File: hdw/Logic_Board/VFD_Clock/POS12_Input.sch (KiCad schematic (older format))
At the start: 29 parts

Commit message: Added display board schematic, other additions to logic board
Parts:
- removed C?: C, symbol Custom_Library:CP_Tant_Custom
- removed D?: D_TVS_ALT, symbol Device:D_TVS_ALT
- added C?: 100uF, Capacitors_Tantalum_SMD:CP_Tantalum_Case-X_EIA-7343-43_Reflow, symbol Custom_Library:CP_Tant_Custom
- added D?: 24V, Diodes_SMD:D_SMA, symbol Device:D_TVS_ALT
- J?: value +24V IN -> +12V IN
- R?: value 1.3M -> 6.04M
- R?: value 4.64k -> 86.6k
- R?: value 25.5k -> 243k
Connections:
- net labels added: +12V, POS12_ISNS, POS12_PGOOD
- net labels removed: +24V, +24Vin, POS24_ISNS, POS24_PGOOD
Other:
- note added: "UVLO threshold set to 10V\nOVLO threshold set to 14V"
- note removed: "UVLO threshold set to 22V\nOVLO threshold set to 26V"

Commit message: Resurrected project
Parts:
- removed C?: 0.1uF, Capacitors_SMD:C_0603, symbol Custom_Library:C_Custom
- removed C?: 10nF, Capacitors_SMD:C_0603, symbol Custom_Library:C_Custom
- removed C? (x2): 1nF, Capacitors_SMD:C_0603, symbol Custom_Library:C_Custom
- removed R?: 499k, Resistors_SMD:R_0603, symbol Custom_Library:R_Custom
- removed TP?: TP, Pin_Headers:Pin_Header_Angled_1x01_Pitch2.54mm, symbol Custom_Library:TP
- removed U?: INA138, TO_SOT_Packages_SMD:SOT-23-5, symbol Amplifier_Current:INA138
- added C?: 0.1uF, Capacitors_SMD:C_0603, symbol Custom_Library:C_Custom
- added R? (x2): 10, Resistors_SMD:R_0603, symbol Custom_Library:R_Custom
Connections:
- net +12V: now also R?.2
- net at Q?.5 (D), R?.1, U?.6 (Vout): now also R?.2
- new net POS12_SNS_+: C?.1, R?.1
- new net POS12_SNS_-: C?.2, R?.1
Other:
- note removed: "1.996 V/A"
- moved on the sheet: C?, R?, TP?

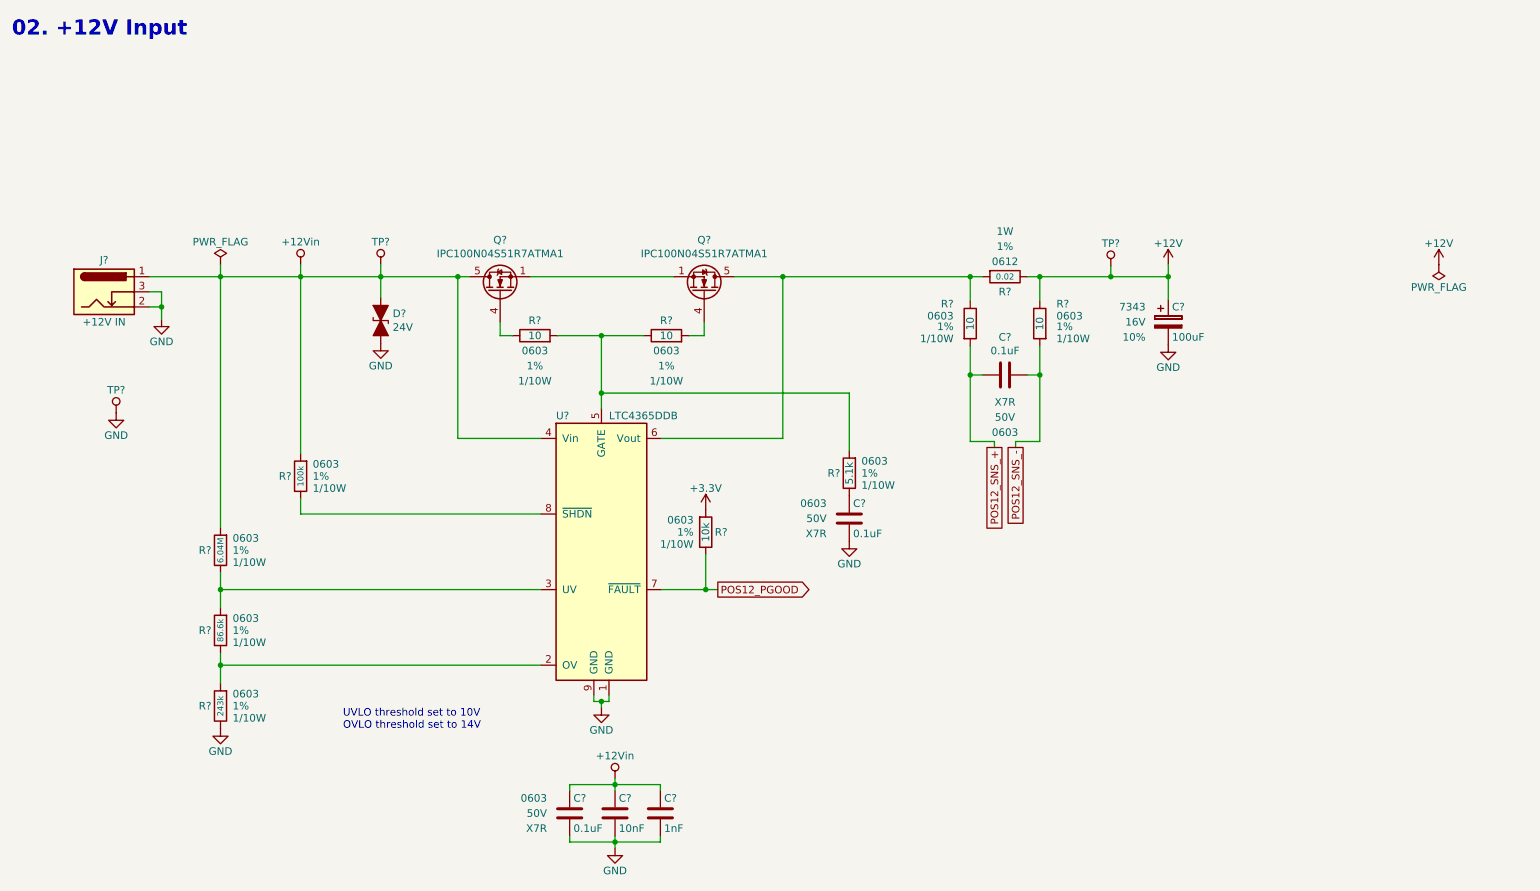
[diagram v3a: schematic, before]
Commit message: Power supply additions
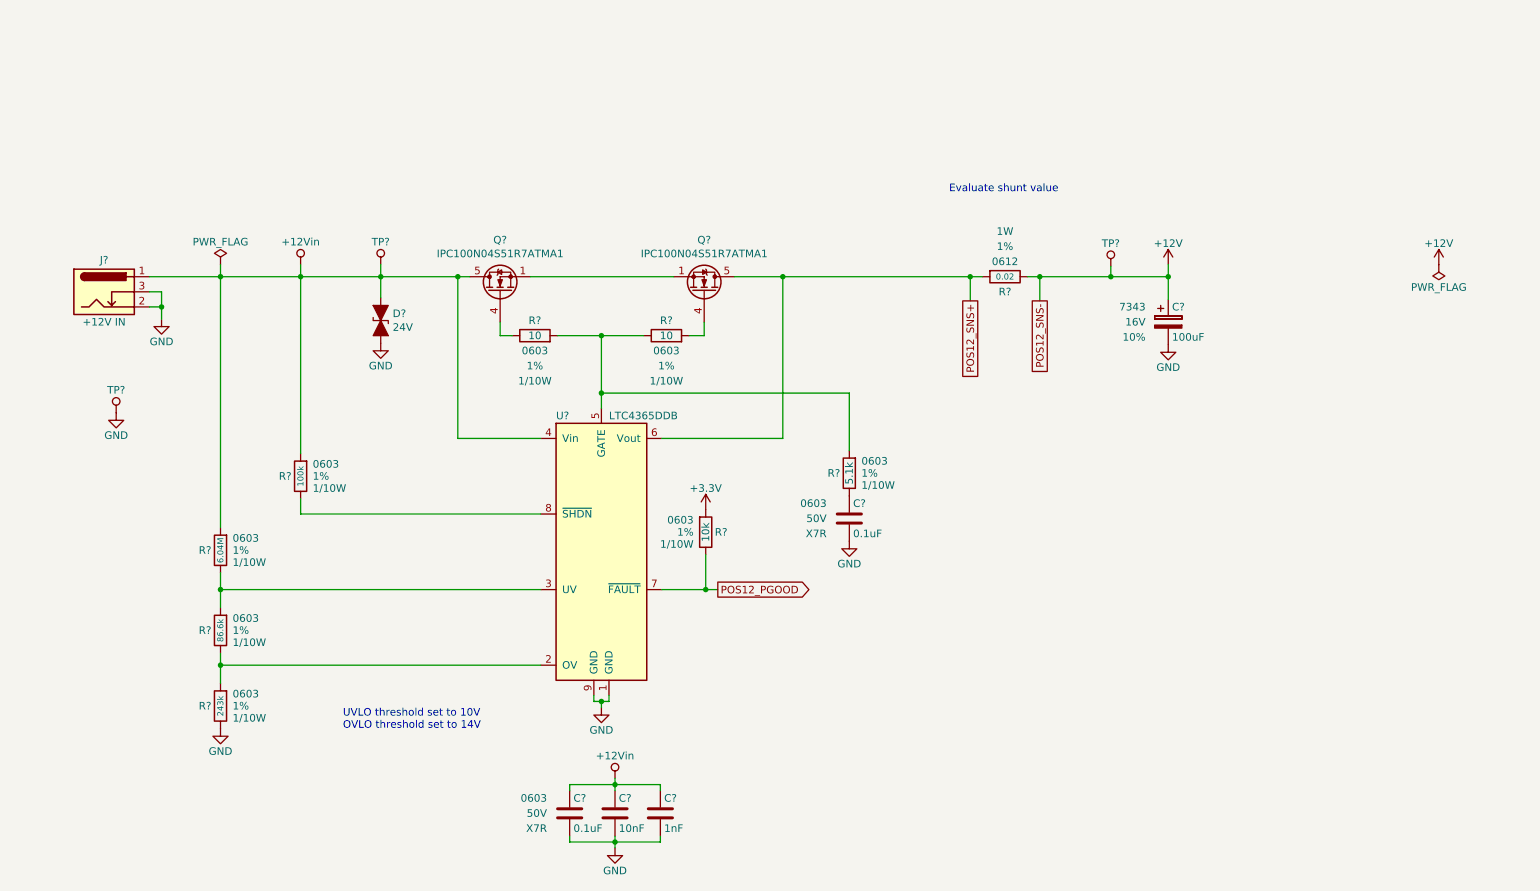
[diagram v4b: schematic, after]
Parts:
- removed C?: 0.1uF, Capacitors_SMD:C_0603, symbol Custom_Library:C_Custom
- removed R? (x2): 10, Resistors_SMD:R_0603, symbol Custom_Library:R_Custom
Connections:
- net POS12_SNS+: now reaches Q?.5 (D), R?.1, U?.6 (Vout)
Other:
- note added: "Evaluate shunt value"
- note removed: "02. +12V Input"
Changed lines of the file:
@@
 $Descr A 11000 8500
 encoding utf-8
-Sheet 16 20
+Sheet 14 25
 Title "QI Charger"
 Date "2019-01-03"
@@
 	7810 2200 7810 2270
 Connection ~ 7810 2270
-Text Notes 540  690  0    100  ~ 20
-02. +12V Input
 $Comp
 L power:+3.3V #PWR?
@@
 $EndComp
 Connection ~ 5640 2270
-Text GLabel 7040 3400 3    50   UnSpc ~ 0
-POS12_SNS_+
-Text GLabel 7180 3400 3    50   UnSpc ~ 0
-POS12_SNS_-
-$Comp
-L Custom_Library:R_Custom R?
-U 1 1 5E074F62
-P 6880 2580
-F 0 "R?" H 6990 2450 50  0000 L CNN
-F 1 "10" V 6880 2580 50  0000 C CNN
-F 2 "Resistors_SMD:R_0603" H 6880 2580 50  0001 C CNN
-F 3 "" H 6880 2580 50  0001 C CNN
-F 4 "YAG3351CT-ND" H 7180 2980 60  0001 C CNN "Digi-Key PN"
-F 5 "0603" H 6990 2530 50  0000 L CNN "display_footprint"
-F 6 "1%" H 6990 2600 50  0000 L CNN "Tolerance"
-F 7 "1/10W" H 6990 2680 50  0000 L CNN "Wattage"
-	1    6880 2580
-	-1   0    0    1
-$EndComp
-$Comp
-L Custom_Library:R_Custom R?
-U 1 1 5E076BDD
-P 7340 2580
-F 0 "R?" H 7450 2450 50  0000 L CNN
-F 1 "10" V 7340 2580 50  0000 C CNN
-F 2 "Resistors_SMD:R_0603" H 7340 2580 50  0001 C CNN
-F 3 "" H 7340 2580 50  0001 C CNN
-F 4 "YAG3351CT-ND" H 7640 2980 60  0001 C CNN "Digi-Key PN"
-F 5 "0603" H 7450 2530 50  0000 L CNN "display_footprint"
-F 6 "1%" H 7450 2600 50  0000 L CNN "Tolerance"
-F 7 "1/10W" H 7450 2680 50  0000 L CNN "Wattage"
-	1    7340 2580
-	1    0    0    1
-$EndComp
-$Comp
-L Custom_Library:C_Custom C?
-U 1 1 5E0794C5
-P 7110 2920
-AR Path="/5BAAE16C/5E0794C5" Ref="C?"  Part="1"
-AR Path="/5BB181D8/5E0794C5" Ref="C?"  Part="1"
-AR Path="/5BB2595E/5E0794C5" Ref="C?"  Part="1"
-AR Path="/5BAAE0FA/5E0794C5" Ref="C?"  Part="1"
-AR Path="/5BB86F23/5E0794C5" Ref="C?"  Part="1"
-AR Path="/5C1D5C9E/5E0794C5" Ref="C?"  Part="1"
-AR Path="/5CB6F1ED/5E0794C5" Ref="C?"  Part="1"
-F 0 "C?" V 7360 2920 50  0000 C CNN
-F 1 "0.1uF" V 7270 2920 50  0000 C CNN
-F 2 "Capacitors_SMD:C_0603" H 7148 2770 50  0001 C CNN
-F 3 "" H 7135 3020 50  0001 C CNN
-F 4 "0603" V 6730 2920 50  0000 C CNN "display_footprint"
-F 5 "50V" V 6830 2920 50  0000 C CNN "Voltage"
-F 6 "X7R" V 6930 2920 50  0000 C CNN "Dielectric"
-F 7 "311-1344-1-ND" H 7535 3420 60  0001 C CNN "Digi-Key PN"
-	1    7110 2920
-	0    -1   -1   0
-$EndComp
-Wire Wire Line
-	6880 2730 6880 2920
-Wire Wire Line
-	6880 2920 6960 2920
-Wire Wire Line
-	7260 2920 7340 2920
-Wire Wire Line
-	7340 2920 7340 2730
-Wire Wire Line
-	6880 2920 6880 3360
-Wire Wire Line
-	6880 3360 7040 3360
-Wire Wire Line
-	7040 3360 7040 3400
-Connection ~ 6880 2920
-Wire Wire Line
-	7340 2920 7340 3360
-Wire Wire Line
-	7340 3360 7180 3360
-Wire Wire Line
-	7180 3360 7180 3400
-Connection ~ 7340 2920
 Wire Wire Line
 	5640 2270 6880 2270
@@
 Wire Wire Line
 	6880 2270 6960 2270
+Text Notes 6740 1720 0    50   ~ 0
+Evaluate shunt value
+Text GLabel 7340 2430 3    50   UnSpc ~ 0
+POS12_SNS-
+Text GLabel 6880 2430 3    50   UnSpc ~ 0
+POS12_SNS+
 $EndSCHEMATC

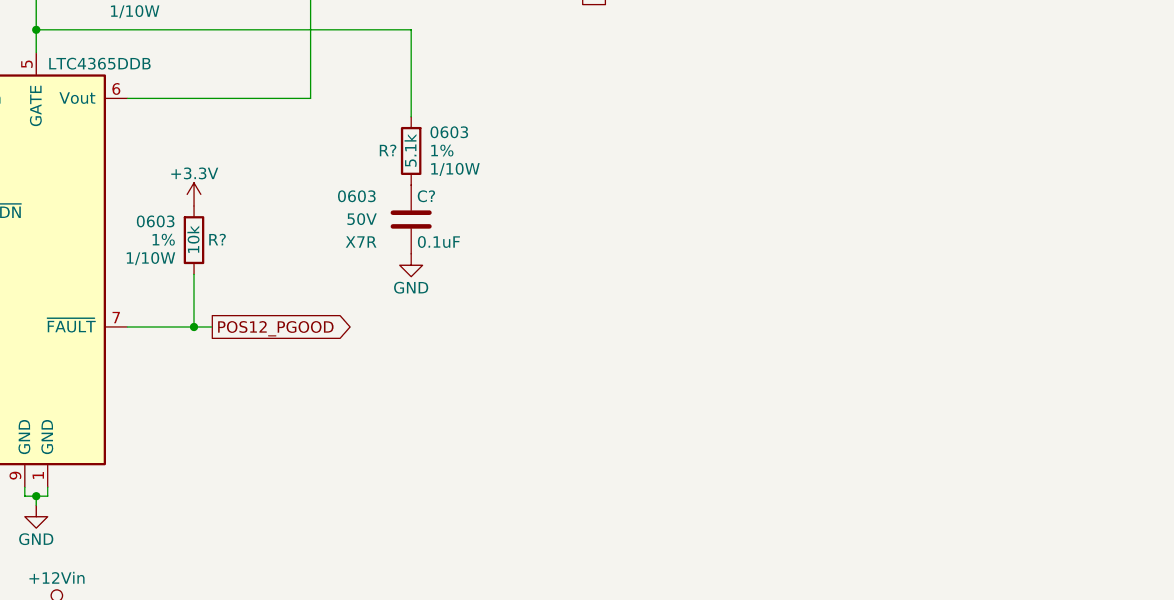
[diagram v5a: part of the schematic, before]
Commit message: Lots of schematic additions
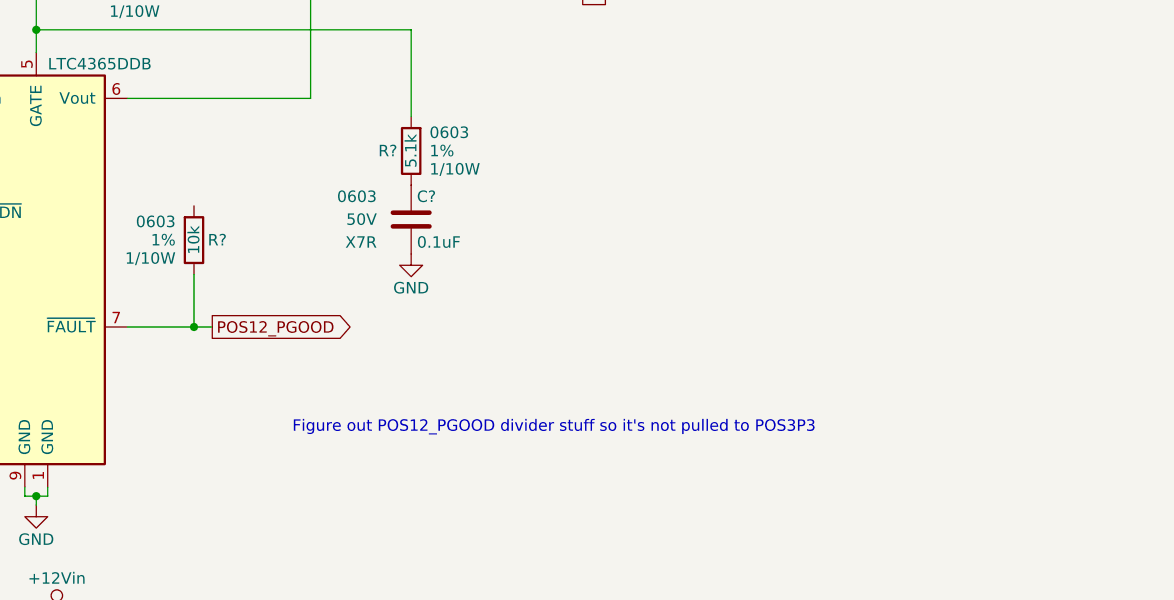
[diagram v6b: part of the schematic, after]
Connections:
- net +3V3: no longer names the net of R?.1
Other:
- note added: "Figure out POS12_PGOOD divider stuff so it's not pulled to POS3P3"
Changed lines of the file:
@@
 $Descr A 11000 8500
 encoding utf-8
-Sheet 14 26
+Sheet 14 28
 Title "QI Charger"
 Date "2019-01-03"
@@
 	7810 2200 7810 2270
 Connection ~ 7810 2270
-$Comp
-L power:+3.3V #PWR?
-U 1 1 5CB6E44A
-P 5130 3810
-F 0 "#PWR?" H 5130 3660 50  0001 C CNN
-F 1 "+3.3V" H 5130 3950 50  0000 C CNN
-F 2 "" H 5130 3810 50  0001 C CNN
-F 3 "" H 5130 3810 50  0001 C CNN
-	1    5130 3810
-	1    0    0    -1
-$EndComp
 Connection ~ 5640 2270
 Wire Wire Line
@@
 Text GLabel 6880 2430 3    50   UnSpc ~ 0
 POS12_SNS+
+Text Notes 5560 4810 0    50   ~ 0
+Figure out POS12_PGOOD divider stuff so it's not pulled to POS3P3
 $EndSCHEMATC

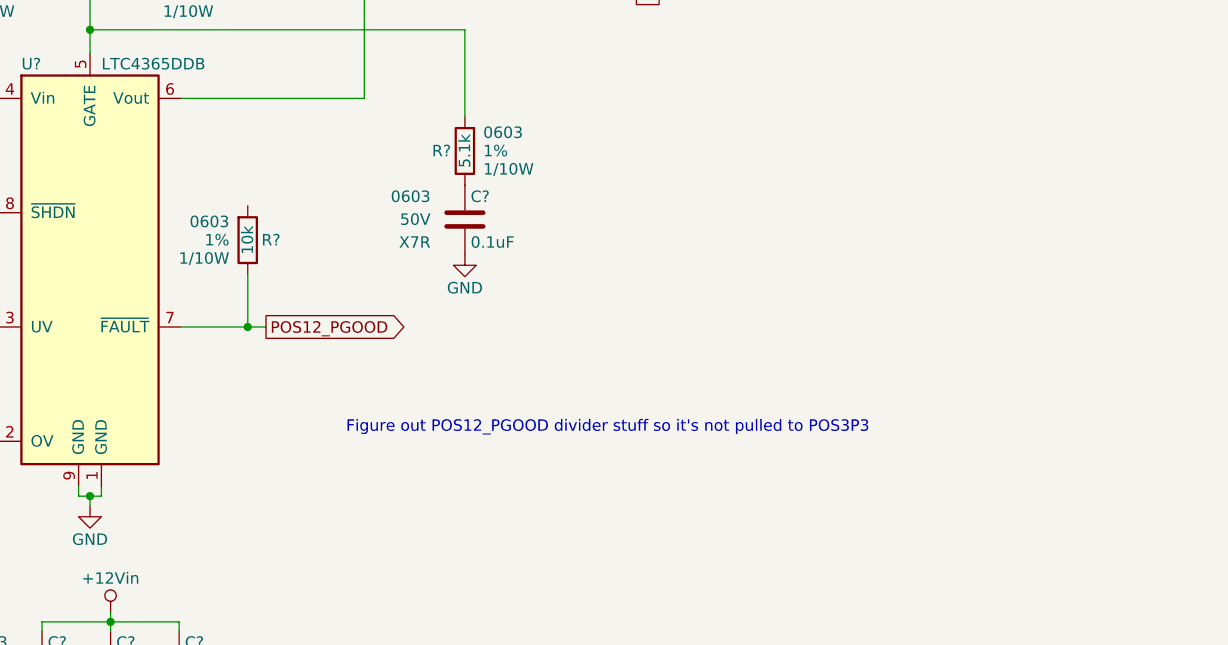
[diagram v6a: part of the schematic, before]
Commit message: Started IV-6 display board, continued logic board development
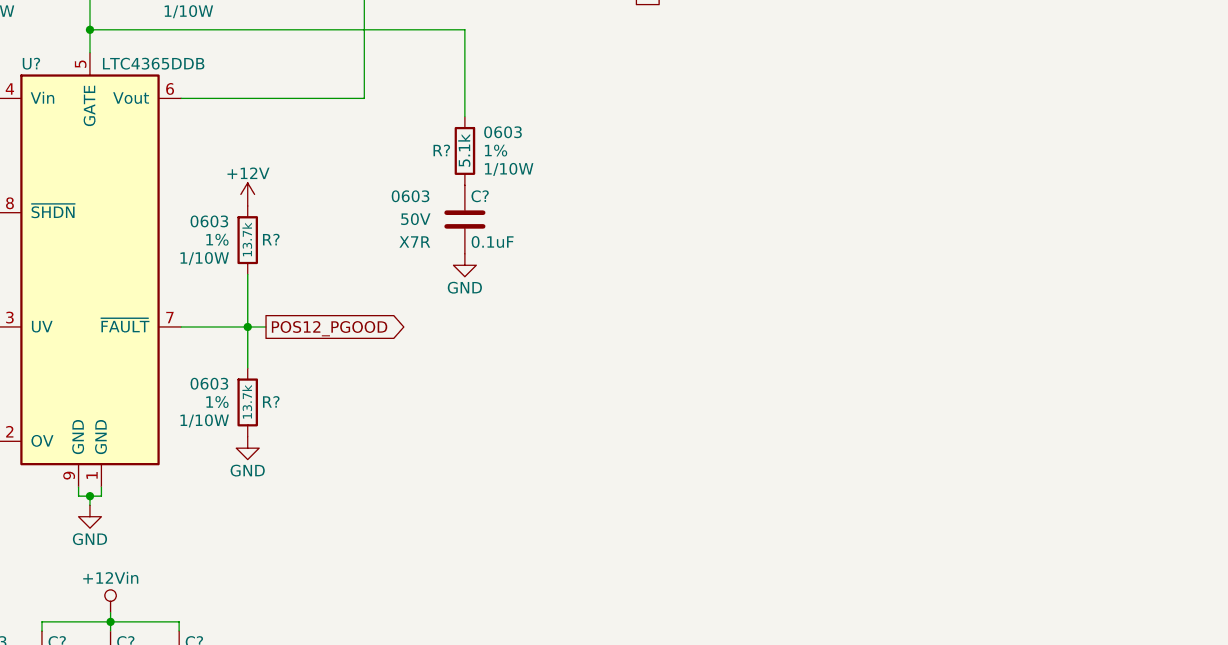
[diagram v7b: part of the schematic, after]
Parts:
- added R?: 13.7k, Resistors_SMD:R_0603, symbol Custom_Library:R_Custom
- R?: value 10k -> 13.7k; Digi-Key PN RMCF0603FT10K0CT-ND -> (none)
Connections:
- net +12V: now also R?.1
- net GND: now also R?.2
- net POS12_PGOOD: now also R?.1
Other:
- note removed: "Figure out POS12_PGOOD divider stuff so it's not pulled to POS3P3"
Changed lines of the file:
@@
 AR Path="/5CB6F1ED/5BB7655D" Ref="R?"  Part="1"
 F 0 "R?" H 5070 3960 50  0000 R CNN
-F 1 "10k" V 5130 3960 50  0000 C CNN
+F 1 "13.7k" V 5130 3960 40  0000 C CNN
 F 2 "Resistors_SMD:R_0603" H 5130 3960 50  0001 C CNN
 F 3 "" H 5130 3960 50  0001 C CNN
-F 4 "RMCF0603FT10K0CT-ND" H 5430 4360 60  0001 C CNN "Digi-Key PN"
-F 5 "0603" H 5210 4040 50  0000 L CNN "display_footprint"
-F 6 "1%" H 5210 3960 50  0000 L CNN "Tolerance"
-F 7 "1/10W" H 5210 3880 50  0000 L CNN "Wattage"
+F 4 "0603" H 5210 4040 50  0000 L CNN "display_footprint"
+F 5 "1%" H 5210 3960 50  0000 L CNN "Tolerance"
+F 6 "1/10W" H 5210 3880 50  0000 L CNN "Wattage"
 	1    5130 3960
 	-1   0    0    -1
@@
 Text GLabel 6880 2430 3    50   UnSpc ~ 0
 POS12_SNS+
-Text Notes 5560 4810 0    50   ~ 0
-Figure out POS12_PGOOD divider stuff so it's not pulled to POS3P3
+$Comp
+L Custom_Library:R_Custom R?
+U 1 1 5E109792
+P 5130 4670
+AR Path="/5BB2595E/5E109792" Ref="R?"  Part="1"
+AR Path="/5BAAE0FA/5E109792" Ref="R?"  Part="1"
+AR Path="/5BB86F23/5E109792" Ref="R?"  Part="1"
+AR Path="/5C1D5C9E/5E109792" Ref="R?"  Part="1"
+AR Path="/5CB6F1ED/5E109792" Ref="R?"  Part="1"
+F 0 "R?" H 5070 4670 50  0000 R CNN
+F 1 "13.7k" V 5130 4670 40  0000 C CNN
+F 2 "Resistors_SMD:R_0603" H 5130 4670 50  0001 C CNN
+F 3 "" H 5130 4670 50  0001 C CNN
+F 4 "0603" H 5210 4750 50  0000 L CNN "display_footprint"
+F 5 "1%" H 5210 4670 50  0000 L CNN "Tolerance"
+F 6 "1/10W" H 5210 4590 50  0000 L CNN "Wattage"
+	1    5130 4670
+	-1   0    0    -1
+$EndComp
+$Comp
+L power:GND #PWR?
+U 1 1 5E109F30
+P 5130 4820
+F 0 "#PWR?" H 5130 4570 50  0001 C CNN
+F 1 "GND" H 5130 4670 50  0000 C CNN
+F 2 "" H 5130 4820 50  0001 C CNN
+F 3 "" H 5130 4820 50  0001 C CNN
+	1    5130 4820
+	1    0    0    -1
+$EndComp
+Wire Wire Line
+	5130 4520 5130 4340
+$Comp
+L power:+12V #PWR?
+U 1 1 5E10B9FF
+P 5130 3810
+F 0 "#PWR?" H 5130 3660 50  0001 C CNN
+F 1 "+12V" H 5130 3950 50  0000 C CNN
+F 2 "" H 5130 3810 50  0001 C CNN
+F 3 "" H 5130 3810 50  0001 C CNN
+	1    5130 3810
+	1    0    0    -1
+$EndComp
 $EndSCHEMATC
